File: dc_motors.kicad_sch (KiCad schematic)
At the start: 20 parts, among them J1 Conn_01x02, J2 Conn_01x02, J3 Conn_01x02, J4 Conn_01x02, Q1 SI2318CDS, Q2 SI2318CDS, Q3 SI2318CDS, Q4 SI2318CDS

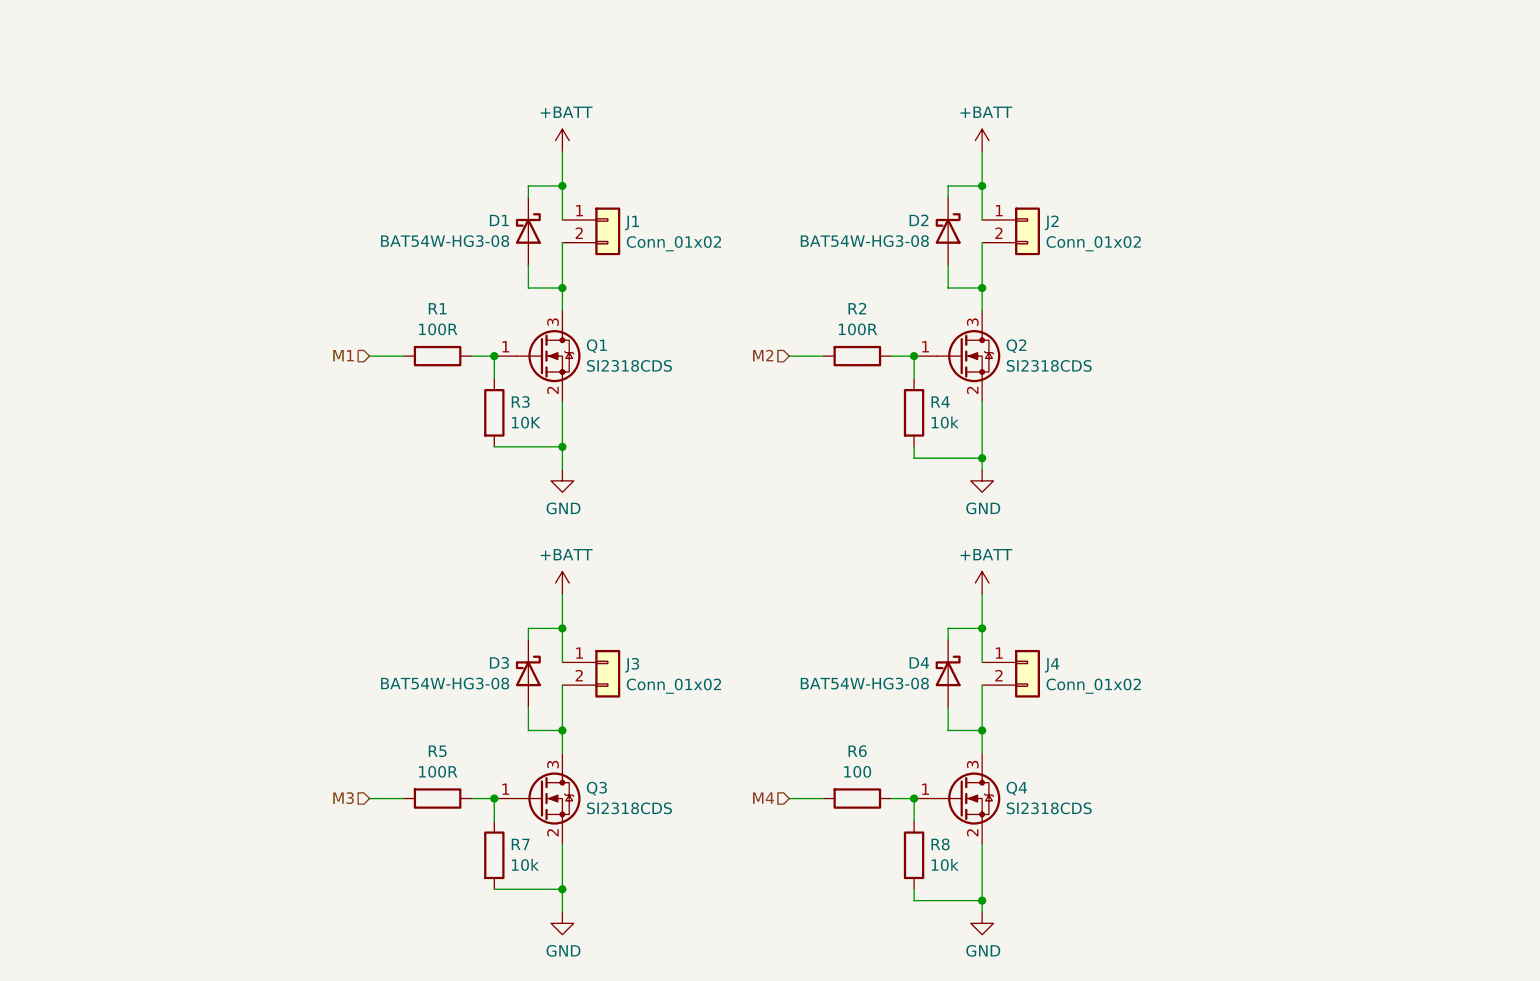
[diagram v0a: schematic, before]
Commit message: Initial schematic version
This is now a clean and ready version of the schematic:
That means:
- Schematic has been reviewed,
- It's fully annotated,
- All elements have been checked for availability with JLCPCB,
- Footprints were assigned,
- ERC is green.

No design changes should be added for this version until
the PCB is present and version is released.
Only bugfixes are possible now.
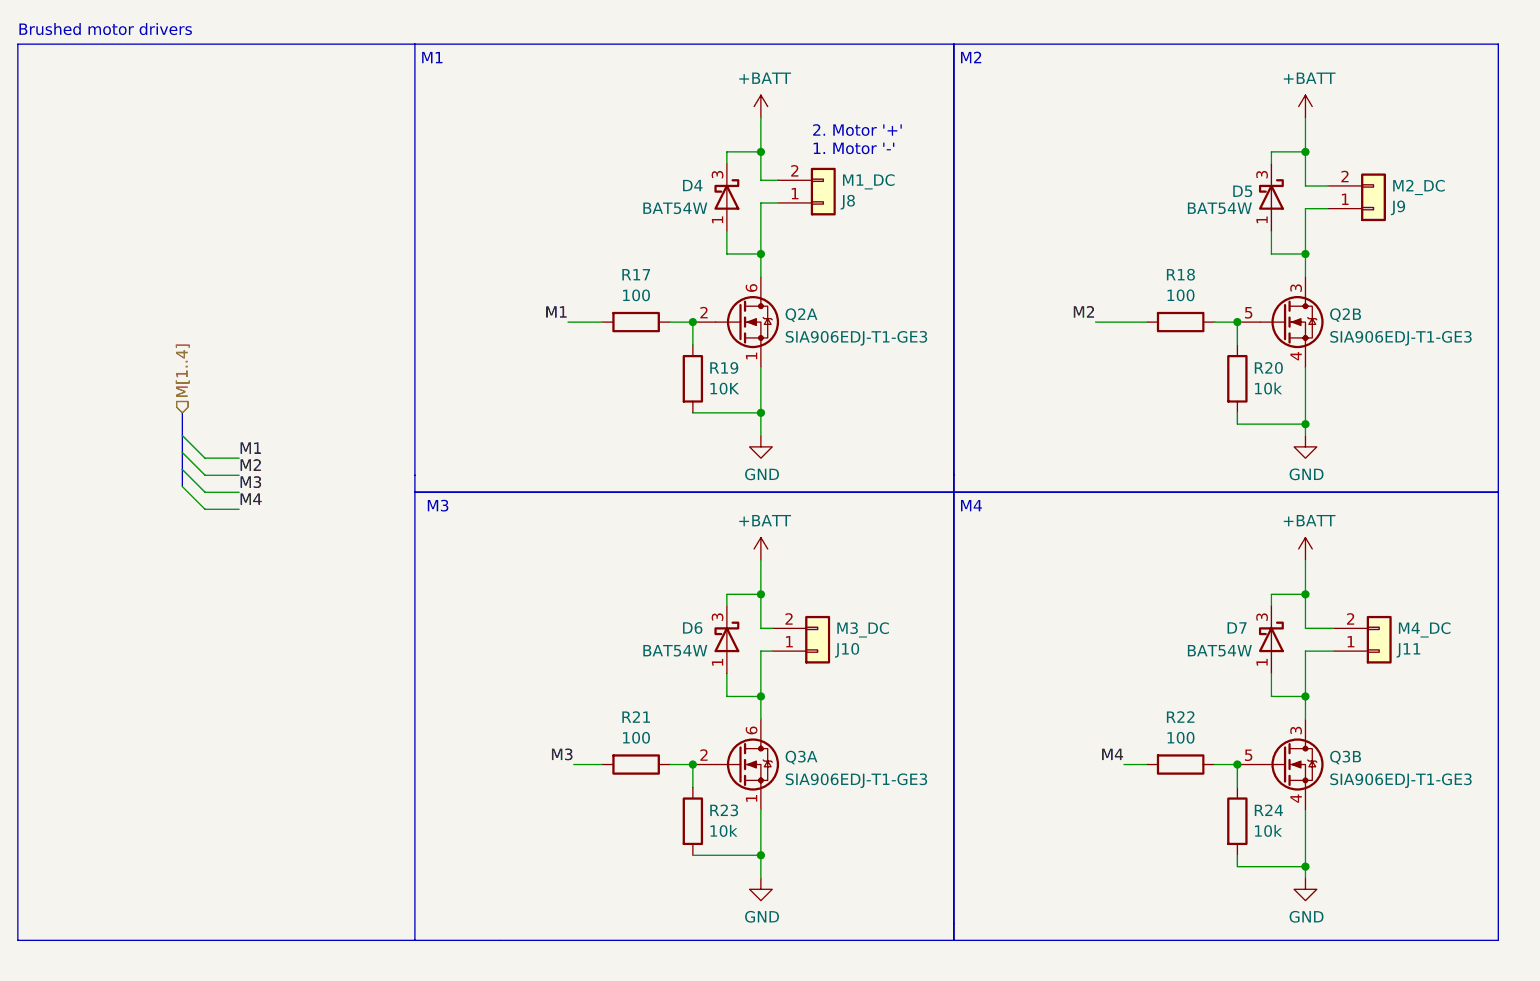
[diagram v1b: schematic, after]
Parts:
- removed D1, D2, D3, D4: BAT54W-HG3-08, Diode_SMD:D_SOD-123, symbol custom:BAT54W-HG3-08
- removed J1, J2, J3, J4: Conn_01x02, Connector_PinSocket_2.00mm:PinSocket_1x02_P2.00mm_Vertical, symbol Connector_Generic:Conn_01x02
- removed Q1, Q2, Q3, Q4: SI2318CDS, Package_TO_SOT_SMD:SOT-23, symbol CustomFET:SI2318CDS
- added D4, D5, D6, D7: BAT54W, Diode_SMD:D_SOD-123, symbol Diode:BAT54W
- added J10: M3_DC, Connector_PinHeader_2.54mm:PinHeader_1x02_P2.54mm_Vertical, symbol Connector_Generic:Conn_01x02
- added J11: M4_DC, Connector_PinHeader_2.54mm:PinHeader_1x02_P2.54mm_Vertical, symbol Connector_Generic:Conn_01x02
- added J8: M1_DC, Connector_PinHeader_2.54mm:PinHeader_1x02_P2.54mm_Vertical, symbol Connector_Generic:Conn_01x02
- added J9: M2_DC, Connector_PinHeader_2.54mm:PinHeader_1x02_P2.54mm_Vertical, symbol Connector_Generic:Conn_01x02
- added Q2, Q3: SIA906EDJ-T1-GE3, Package_TO_SOT_SMD:Vishay_PowerPAK_SC70-6L_Dual, symbol Device:Q_Dual_NMOS_S1G1D2S2G2D1
- R17: renamed from R1; value 100R -> 100
- R18: renamed from R2; value 100R -> 100
- R21: renamed from R5; value 100R -> 100
- renumbered R3 to R19, R4 to R20, R6 to R22, R7 to R23, R8 to R24
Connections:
- net +BATT: now also D4.3 (K), D5.3 (K), D6.3 (K), D7.3 (K), J10.2 (Pin_2), J11.2 (Pin_2), J8.2 (Pin_2), J9.2 (Pin_2)
- net GND: now also Q2.1 (S), Q2.4 (S), Q3.1 (S), Q3.4 (S)
- net at R17.1, R19.1: now also Q2.2 (G)
- net at R18.1, R20.1: now also Q2.5 (G)
- net at R21.1, R23.1: now also Q3.2 (G)
- net at R22.1, R24.1: now also Q3.5 (G)
- new net: D5.1 (A), J9.1 (Pin_1), Q2.3 (D)
- new net: D6.1 (A), J10.1 (Pin_1), Q3.6 (D)
- new net: D4.1 (A), J8.1 (Pin_1), Q2.6 (D)
- new net: D7.1 (A), J11.1 (Pin_1), Q3.3 (D)
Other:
- note added: "2. Motor '+' 1. Motor '-'"
- note added: "Brushed motor drivers"
- note added: "M1"
- note added: "M2"
- note added: "M3"
- note added: "M4"
- moved on the sheet: R17, R18, R19, R20, R21, R22, R23, R24

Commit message: Update footprints and add JLCPCB fields
Update some footprints which will suit better building the pcb
with JLCBPCB. Add fields to components sourced from JLCPCB
to be able to generate BOM.
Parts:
- D4, D5, D6, D7: JLC (none) -> SOD-123; LCSC (none) -> C915628
- Q2, Q3: JLC (none) -> WSON-6-EP(2x2); LCSC (none) -> C142544
- R17, R18, R21, R22: JLC (none) -> 0402; LCSC (none) -> C25076
- R19: value 10K -> 10k; JLC (none) -> 0402
- R20, R23, R24: JLC (none) -> 0402; LCSC (none) -> C25744
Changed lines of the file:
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@@
+      (effects (font (size 1.27 1.27)) hide)
+    )
+    (property "JLC" "0402" (id 4) (at 127.635 73.66 0)
+      (effects (font (size 1.27 1.27)) hide)
+    )
+    (property "LCSC" " C25076" (id 5) (at 127.635 73.66 0)
       (effects (font (size 1.27 1.27)) hide)
     )
@@
       (effects (font (size 1.27 1.27)) hide)
     )
+    (property "JLC" "0402" (id 4) (at 188.595 73.66 0)
+      (effects (font (size 1.27 1.27)) hide)
+    )
+    (property "LCSC" " C25076" (id 5) (at 188.595 73.66 0)
+      (effects (font (size 1.27 1.27)) hide)
+    )
     (pin "1")
     (pin "2")
@@
       (effects (font (size 1.27 1.27)) (justify left))
     )
-    (property "Value" "10K" (id 1) (at 135.763 81.153 0)
+    (property "Value" "10k" (id 1) (at 135.763 81.153 0)
       (effects (font (size 1.27 1.27)) (justify left))
     )
@@
       (effects (font (size 1.27 1.27)) hide)
     )
+    (property "JLC" "0402" (id 4) (at 133.985 80.01 0)
+      (effects (font (size 1.27 1.27)) hide)
+    )
     (pin "1")
     (pin "2")
@@
     )
     (property "Datasheet" "~" (id 3) (at 194.945 80.01 0)
+      (effects (font (size 1.27 1.27)) hide)
+    )
+    (property "JLC" "0402" (id 4) (at 194.945 80.01 0)
+      (effects (font (size 1.27 1.27)) hide)
+    )
+    (property "LCSC" " C25744" (id 5) (at 194.945 80.01 0)
       (effects (font (size 1.27 1.27)) hide)
     )
@@
       (effects (font (size 1.27 1.27)) hide)
     )
+    (property "JLC" "0402" (id 4) (at 127.635 123.19 0)
+      (effects (font (size 1.27 1.27)) hide)
+    )
+    (property "LCSC" " C25076" (id 5) (at 127.635 123.19 0)
+      (effects (font (size 1.27 1.27)) hide)
+    )
     (pin "1")
     (pin "2")
@@
       (effects (font (size 1.27 1.27)) hide)
     )
+    (property "JLC" "0402" (id 4) (at 188.595 123.19 0)
+      (effects (font (size 1.27 1.27)) hide)
+    )
+    (property "LCSC" " C25076" (id 5) (at 188.595 123.19 0)
+      (effects (font (size 1.27 1.27)) hide)
+    )
     (pin "1")
     (pin "2")
@@
       (effects (font (size 1.27 1.27)) hide)
     )
+    (property "JLC" "0402" (id 4) (at 133.985 129.54 0)
+      (effects (font (size 1.27 1.27)) hide)
+    )
+    (property "LCSC" " C25744" (id 5) (at 133.985 129.54 0)
+      (effects (font (size 1.27 1.27)) hide)
+    )
     (pin "1")
     (pin "2")
@@
     )
     (property "Datasheet" "~" (id 3) (at 194.945 129.54 0)
+      (effects (font (size 1.27 1.27)) hide)
+    )
+    (property "JLC" "0402" (id 4) (at 194.945 129.54 0)
+      (effects (font (size 1.27 1.27)) hide)
+    )
+    (property "LCSC" " C25744" (id 5) (at 194.945 129.54 0)
       (effects (font (size 1.27 1.27)) hide)
     )
@@
       (effects (font (size 1.27 1.27)) hide)
     )
+    (property "JLC" "WSON-6-EP(2x2)" (id 4) (at 200.025 73.66 0)
+      (effects (font (size 1.27 1.27)) hide)
+    )
+    (property "LCSC" "C142544" (id 5) (at 200.025 73.66 0)
+      (effects (font (size 1.27 1.27)) hide)
+    )
     (pin "1")
     (pin "2")
@@
       (effects (font (size 1.27 1.27)) hide)
     )
+    (property "JLC" "WSON-6-EP(2x2)" (id 4) (at 139.065 123.19 0)
+      (effects (font (size 1.27 1.27)) hide)
+    )
+    (property "LCSC" "C142544" (id 5) (at 139.065 123.19 0)
+      (effects (font (size 1.27 1.27)) hide)
+    )
     (pin "1")
     (pin "2")
@@
       (effects (font (size 1.27 1.27)) hide)
     )
+    (property "JLC" "SOD-123" (id 4) (at 198.755 59.69 0)
+      (effects (font (size 1.27 1.27)) hide)
+    )
+    (property "LCSC" "C915628" (id 5) (at 198.755 59.69 0)
+      (effects (font (size 1.27 1.27)) hide)
+    )
     (pin "1")
     (pin "2")
@@
       (effects (font (size 1.27 1.27)) hide)
     )
+    (property "JLC" "SOD-123" (id 4) (at 137.795 59.69 0)
+      (effects (font (size 1.27 1.27)) hide)
+    )
+    (property "LCSC" "C915628" (id 5) (at 137.795 59.69 0)
+      (effects (font (size 1.27 1.27)) hide)
+    )
     (pin "1")
     (pin "2")
@@
     )
     (property "Datasheet" "https://assets.nexperia.com/documents/data-sheet/BAT54W_SER.pdf" (id 3) (at 198.755 109.22 0)
+      (effects (font (size 1.27 1.27)) hide)
+    )
+    (property "JLC" "SOD-123" (id 4) (at 198.755 109.22 0)
+      (effects (font (size 1.27 1.27)) hide)
+    )
+    (property "LCSC" "C915628" (id 5) (at 198.755 109.22 0)
       (effects (font (size 1.27 1.27)) hide)
     )
@@
       (effects (font (size 1.27 1.27)) hide)
     )
+    (property "JLC" "WSON-6-EP(2x2)" (id 4) (at 139.065 73.66 0)
+      (effects (font (size 1.27 1.27)) hide)
+    )
+    (property "LCSC" "C142544" (id 5) (at 139.065 73.66 0)
+      (effects (font (size 1.27 1.27)) hide)
+    )
     (pin "1")
     (pin "2")
@@
       (effects (font (size 1.27 1.27)) hide)
     )
+    (property "JLC" "WSON-6-EP(2x2)" (id 4) (at 200.025 123.19 0)
+      (effects (font (size 1.27 1.27)) hide)
+    )
+    (property "LCSC" "C142544" (id 5) (at 200.025 123.19 0)
+      (effects (font (size 1.27 1.27)) hide)
+    )
     (pin "1")
     (pin "2")
@@
       (effects (font (size 1.27 1.27)) hide)
     )
+    (property "JLC" "SOD-123" (id 4) (at 137.795 109.22 0)
+      (effects (font (size 1.27 1.27)) hide)
+    )
+    (property "LCSC" "C915628" (id 5) (at 137.795 109.22 0)
+      (effects (font (size 1.27 1.27)) hide)
+    )
